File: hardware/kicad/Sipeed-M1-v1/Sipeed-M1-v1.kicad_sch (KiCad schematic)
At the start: 157 parts, among them IC1 TROPIC01_chip, J1 USB_C_, J2 JST Connector, J3 Conn_02x20_Odd_Even, J4 Conn_01x09_Pin, J5 Conn_02x03_Odd_Even, J7 Conn_01x30_Pin, SW1 SW_Push, SW10 SW_Push, SW11 SW_Push, SW12 SW_Push, SW13 SW_Push, SW14 SW_Push, SW15 SW_Push, SW16 SW_Push, SW2 SW_Push, SW3 SW_Push, SW4 SW_Push, SW5 SW_Push, SW6 SW_Push, SW7 SW_Push, SW8 SW_Push, SW9 SW_Push, U1 Sipeed-M1, U2 ESP32-S3-WROOM-1U-N8R8, U3 PAM2401YPADJ, U4 TPS63070RNMR, U5 MCP23017_SO, U7 USBLC6-2SC6, U8 MCP73871

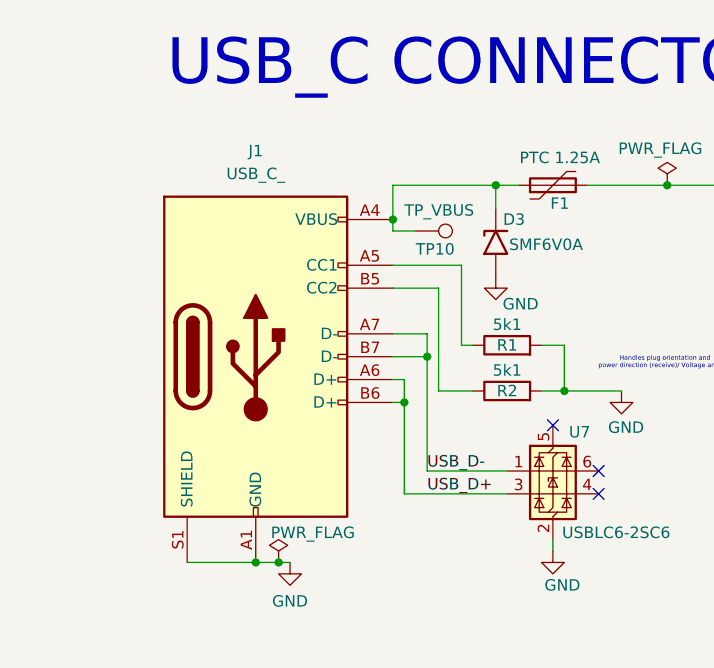
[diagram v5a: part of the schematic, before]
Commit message: USB-C connector now using SHOU HAN TYPE-C 16PIN 2MD(073)
Adding footprint and 3D model.
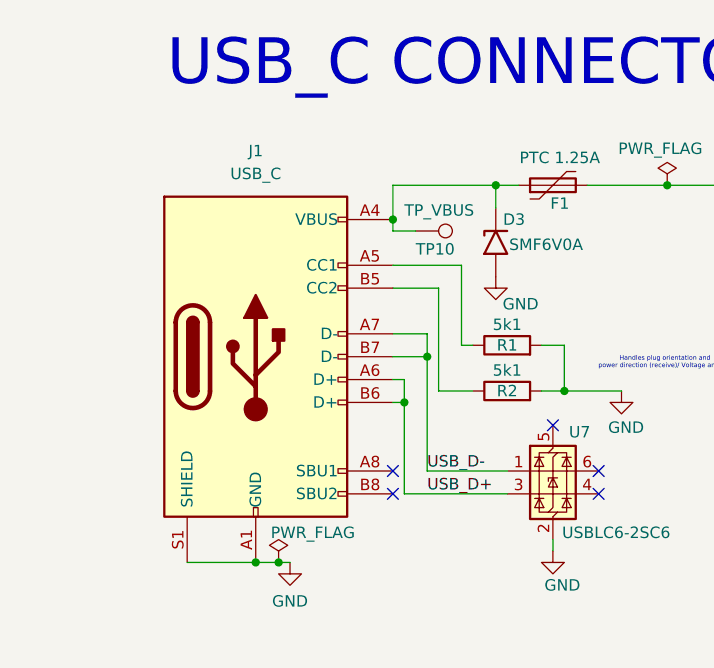
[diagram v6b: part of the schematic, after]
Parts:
- J1: value USB_C_ -> USB_C; footprint Connector_USB:USB_C_Receptacle_HRO_TYPE-C-31-M-12 -> _M1_FP_lib:SHOUHAN_TYPE-C_16PIN_2MD__073_; symbol _M1_symbols:USB_C_Receptacle_USB2.0_14P -> Connector:USB_C_Receptacle_USB2.0_16P; JLCPCB PN (none) -> C2765186
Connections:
- no-connect marks 42 -> 44
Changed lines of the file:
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@@
 	)
 	(no_connect
+		(at 69.85 82.55)
+	)
+	(no_connect
 		(at 62.23 342.9)
 	)
@@
 	)
 	(no_connect
+		(at 69.85 80.01)
+	)
+	(no_connect
 		(at 62.23 363.22)
 	)
@@
 	)
 	(symbol
-		(lib_id "_M1_symbols:USB_C_Receptacle_USB2.0_14P")
+		(lib_id "Connector:USB_C_Receptacle_USB2.0_16P")
 		(at 54.61 67.31 0)
 		(unit 1)
@@
 			)
 		)
-		(property "Value" "USB_C_"
+		(property "Value" "USB_C"
 			(at 54.61 46.99 0)
 			(effects
@@
 			)
 		)
-		(property "Footprint" "Connector_USB:USB_C_Receptacle_HRO_TYPE-C-31-M-12"
+		(property "Footprint" "_M1_FP_lib:SHOUHAN_TYPE-C_16PIN_2MD__073_"
 			(at 58.42 67.31 0)
 			(effects
@@
 			)
 		)
-		(property "Description" "USB 2.0-only 14P Type-C Receptacle connector"
+		(property "Description" "USB 2.0-only 16P Type-C Receptacle connector"
+			(at 54.61 67.31 0)
+			(effects
+				(font
+					(size 1.27 1.27)
+				)
+				(hide yes)
+			)
+		)
+		(property "JLCPCB PN" "C2765186"
 			(at 54.61 67.31 0)
 			(effects
@@
 		(pin "B5"
 		)
+		(pin "A8"
+		)
+		(pin "B8"
+		)
 		(instances

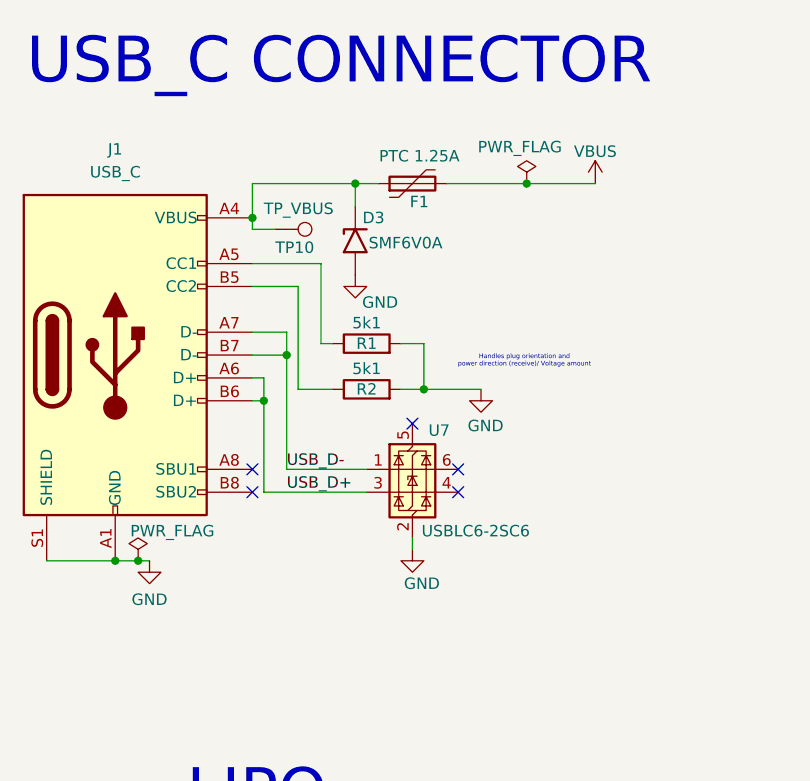
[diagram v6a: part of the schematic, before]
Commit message: ESD protection: fix connections, add JLCPCB PN
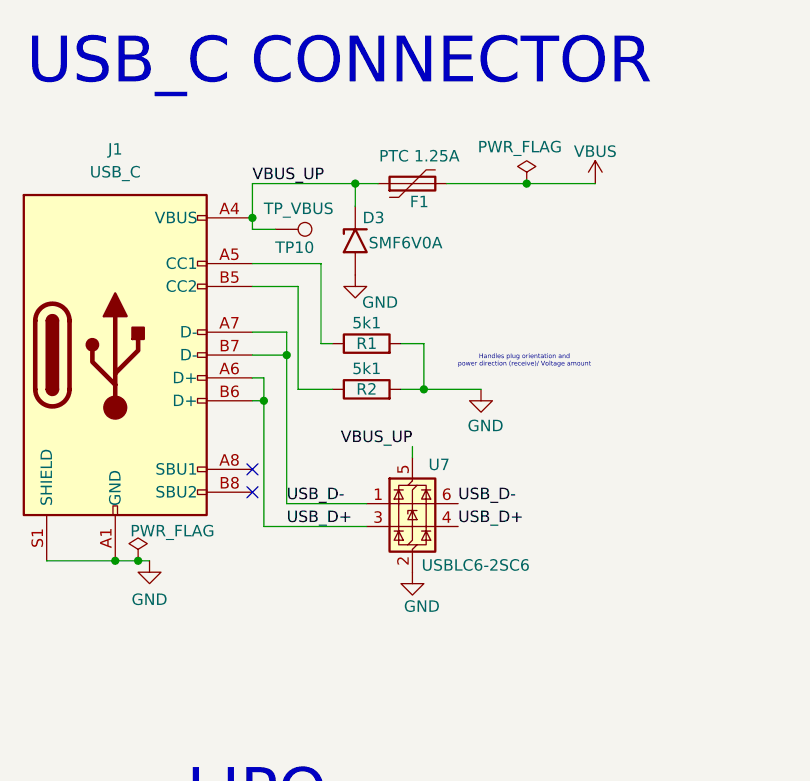
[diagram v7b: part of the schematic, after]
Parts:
- U7: JLCPCB PN (none) -> C7519
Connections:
- net USB_D+: now also U7.4 (I/O2)
- net USB_D-: now also U7.6 (I/O1)
- net VBUS_UP: now reaches U7.5 (VBUS)
- net VBUS_UP: now also D3.1 (A1), F1.1, J1.A4 (VBUS), J1.A9 (VBUS), J1.B4 (VBUS), J1.B9 (VBUS), TP10.1
- no-connect marks 44 -> 41
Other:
- moved on the sheet: U7
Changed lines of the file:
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@@
 	)
 	(no_connect
-		(at 87.63 74.93)
-	)
-	(no_connect
 		(at 191.77 214.63)
 	)
@@
 	)
 	(no_connect
-		(at 92.71 80.01)
-	)
-	(no_connect
 		(at 62.23 317.5)
 	)
@@
 	)
 	(no_connect
-		(at 92.71 82.55)
-	)
-	(no_connect
 		(at 62.23 307.34)
 	)
@@
 	(wire
 		(pts
-			(xy 71.12 72.39) (xy 71.12 82.55)
+			(xy 71.12 72.39) (xy 71.12 86.36)
 		)
 		(stroke
@@
 	(wire
 		(pts
-			(xy 73.66 67.31) (xy 73.66 80.01)
+			(xy 73.66 67.31) (xy 73.66 83.82)
 		)
 		(stroke
@@
 	(wire
 		(pts
-			(xy 73.66 80.01) (xy 82.55 80.01)
+			(xy 73.66 83.82) (xy 82.55 83.82)
 		)
 		(stroke
@@
 	(wire
 		(pts
-			(xy 71.12 82.55) (xy 82.55 82.55)
+			(xy 71.12 86.36) (xy 82.55 86.36)
 		)
 		(stroke
@@
 	(wire
 		(pts
+			(xy 87.63 77.47) (xy 87.63 78.74)
+		)
+		(stroke
+			(width 0)
+			(type default)
+		)
+	)
+	(wire
+		(pts
 			(xy 220.98 185.42) (xy 224.79 185.42)
 		)
@@
 	(wire
 		(pts
-			(xy 87.63 87.63) (xy 87.63 88.9)
-		)
-		(stroke
-			(width 0)
-			(type default)
-		)
-	)
-	(wire
-		(pts
 			(xy 229.87 316.23) (xy 243.84 316.23)
 		)
@@
 		)
 	)
+	(label "USB_D-"
+		(at 92.71 83.82 0)
+		(effects
+			(font
+				(size 1.27 1.27)
+			)
+			(justify left bottom)
+		)
+	)
 	(label "M1_MIC_DAT3"
 		(at 152.4 336.55 0)
@@
 	)
 	(label "USB_D-"
-		(at 73.66 80.01 0)
+		(at 73.66 83.82 0)
 		(effects
 			(font
@@
 		)
 	)
+	(label "USB_D+"
+		(at 92.71 86.36 0)
+		(effects
+			(font
+				(size 1.27 1.27)
+			)
+			(justify left bottom)
+		)
+	)
 	(label "M1_MIC_DAT1"
 		(at 152.4 341.63 0)
@@
 		)
 	)
+	(label "VBUS_UP"
+		(at 87.63 77.47 180)
+		(effects
+			(font
+				(size 1.27 1.27)
+			)
+			(justify right bottom)
+		)
+	)
 	(label "SPI_MISO"
 		(at 152.4 349.25 0)
@@
 		)
 	)
+	(label "VBUS_UP"
+		(at 69.85 48.26 0)
+		(effects
+			(font
+				(size 1.27 1.27)
+			)
+			(justify left bottom)
+		)
+	)
 	(label "BTN_6"
 		(at 317.5 189.23 0)
@@
 	)
 	(label "USB_D+"
-		(at 73.66 82.55 0)
+		(at 73.66 86.36 0)
 		(effects
 			(font
@@
 	(symbol
 		(lib_id "power:GND")
-		(at 87.63 88.9 0)
+		(at 87.63 91.44 0)
 		(unit 1)
 		(exclude_from_sim no)
@@
 		(dnp no)
 		(property "Reference" "#PWR011"
-			(at 87.63 95.25 0)
+			(at 87.63 97.79 0)
 			(effects
 				(font
@@
 		)
 		(property "Value" "GND"
-			(at 90.678 92.71 0)
+			(at 90.678 95.25 0)
 			(effects
 				(font
@@
 		)
 		(property "Footprint" ""
-			(at 87.63 88.9 0)
+			(at 87.63 91.44 0)
 			(effects
 				(font
@@
 		)
 		(property "Datasheet" ""
-			(at 87.63 88.9 0)
+			(at 87.63 91.44 0)
 			(effects
 				(font
@@
 		)
 		(property "Description" "Power symbol creates a global label with name \"GND\" , ground"
-			(at 87.63 88.9 0)
+			(at 87.63 91.44 0)
 			(effects
 				(font
@@
 	(symbol
 		(lib_id "Power_Protection:USBLC6-2SC6")
-		(at 87.63 80.01 0)
+		(at 87.63 83.82 0)
 		(unit 1)
 		(exclude_from_sim no)
@@
 		(dnp no)
 		(property "Reference" "U7"
-			(at 89.408 75.692 0)
+			(at 89.408 79.502 0)
 			(effects
 				(font
@@
 		)
 		(property "Value" "USBLC6-2SC6"
-			(at 88.646 86.868 0)
+			(at 88.646 90.678 0)
 			(effects
 				(font
@@
 		)
 		(property "Footprint" "Package_TO_SOT_SMD:SOT-23-6"
-			(at 88.9 86.36 0)
+			(at 88.9 90.17 0)
 			(effects
 				(font
@@
 		)
 		(property "Datasheet" "https://www.st.com/resource/en/datasheet/usblc6-2.pdf"
-			(at 88.9 88.265 0)
+			(at 88.9 92.075 0)
 			(effects
 				(font
@@
 		)
 		(property "Description" "Very low capacitance ESD protection diode, 2 data-line, SOT-23-6"
-			(at 87.63 80.01 0)
+			(at 87.63 83.82 0)
+			(effects
+				(font
+					(size 1.27 1.27)
+				)
+				(hide yes)
+			)
+		)
+		(property "JLCPCB PN" "C7519"
+			(at 87.63 83.82 0)
 			(effects
 				(font

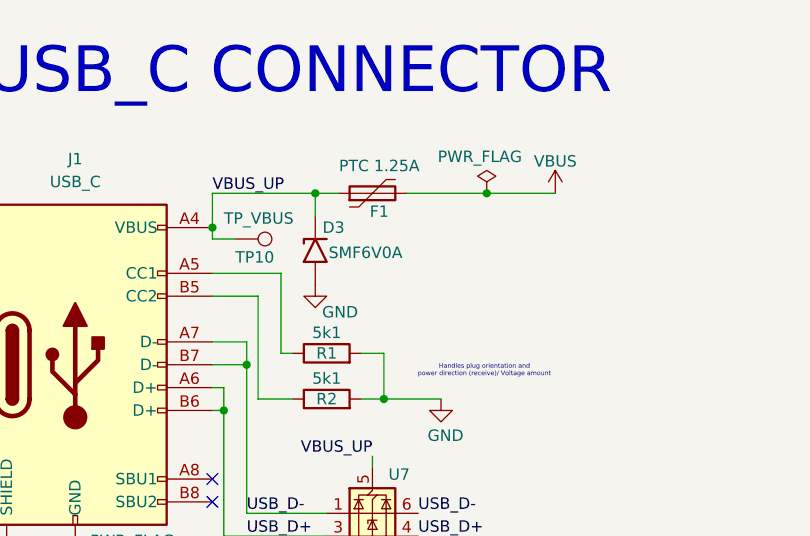
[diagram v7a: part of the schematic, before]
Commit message: ESD protection diode: opt for 5V version
Adding JLCPC PN
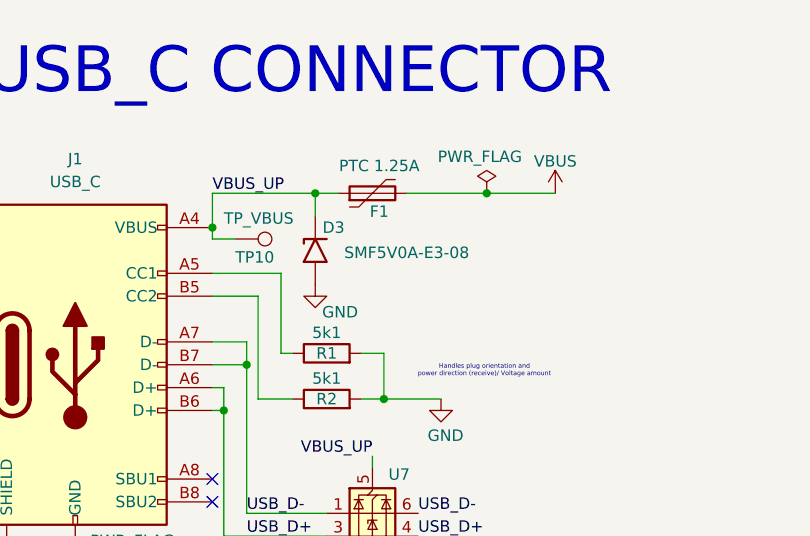
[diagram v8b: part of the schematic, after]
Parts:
- D3: value SMF6V0A -> SMF5V0A-E3-08; JLCPCB PN (none) -> C1972946
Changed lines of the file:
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@@
 			)
 		)
-		(property "Value" "SMF6V0A"
-			(at 86.868 54.864 90)
+		(property "Value" "SMF5V0A-E3-08"
+			(at 91.44 54.864 90)
 			(effects
 				(font
@@
 			(effects
 				(font
+					(size 1.27 1.27)
+				)
+				(hide yes)
+			)
+		)
+		(property "JLCPCB PN" "C1972946"
+			(at 81.28 54.61 90)
+			(effects
+				(font
